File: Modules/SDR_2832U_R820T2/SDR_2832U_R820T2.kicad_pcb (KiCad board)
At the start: 2 copper layers, 140 parts, among them J1 2.54 Pins, J10 2.54 Pins, J2 2.54 Pins, J3 SMA, J4 SMA, J5 USB_C_Receptacle_USB2.0_16P, J6 SMA, J7 SMA, J8 SMA, J9 2.54 Sockets, Q1 GSFJ0300, T1 DXW21BN2511NL, U1 NCV68061, U2 NCV68061, U3 LM66200, U4 R820T2, U5 AP2127K-ADJ, U6 RTL2832U, U7 M24C02-WMN

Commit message: PCB progress
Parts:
- added C49: 100n, libraries:Worthington_C_Narrow_0201, F.Cu at (188.6, 72.3)
- added C50: 100n, libraries:Worthington_C_Narrow_0201, F.Cu at (192.6, 70.9)
- added C51: 100n, libraries:Worthington_C_Narrow_0201, F.Cu at (188.6, 74.6)
- added C52: 47u, libraries:Worthington_C_Narrow_0603, F.Cu at (199.4, 61.4)
- C10, C11, C12, C13, C14, C15, C17, C18, C19, C20, C22, C27, C28, C29, C3, C30, C31, C32, C33, C34, C35, C36, C37, C38, C39, C40, C41, C42, C43, C44, C45, C46, C47, C48, C6, C7, C8, C9: footprint libraries:Worthington_C_0201 -> libraries:Worthington_C_Narrow_0201
- C16, C21, C24, C25, C26, C4, C5: footprint libraries:Worthington_C_0402 -> libraries:Worthington_C_Narrow_0402
- C2: footprint libraries:Worthington_C_0402_0603 -> libraries:Worthington_C_Narrow_0402_0603
- J1, J2: moved to B.Cu
- J3, J6, J7: footprint Connector_Coaxial:SMA_Molex_73251-2200_Horizontal -> Connector_Coaxial:SMA_Amphenol_132289_EdgeMount
- J4: renamed from J8; footprint Connector_Coaxial:SMA_Molex_73251-2200_Horizontal -> Connector_Coaxial:SMA_Amphenol_132289_EdgeMount
- J5: footprint Connector_USB:USB_C_Receptacle_Amphenol_124019772112A -> Connector_USB:USB_C_Receptacle_GCT_USB4105-xx-A_16P_TopMnt_Horizontal
- J8: renamed from J4; footprint Connector_Coaxial:SMA_Molex_73251-2200_Horizontal -> Connector_Coaxial:SMA_Amphenol_132289_EdgeMount
- L1, L2, L3: footprint libraries:Worthington_L_0603_RF -> libraries:Worthington_L_Narrow_0603_RF
- R1, R10, R11, R12, R13, R14, R15, R16, R17, R18, R19, R2, R20, R21, R22, R23, R24, R25, R26, R27, R28, R29, R3, R4, R5, R6, R7, R8, R9: footprint libraries:Worthington_R_0201 -> libraries:Worthington_R_Narrow_0201
- moved J3 130.7 mm to (215.8, 86.9)
- moved C12 110.4 mm to (195.0, 79.3)
- moved C34 109.5 mm to (198.5, 62.2), turned to 90 degrees
- moved C15 109.4 mm to (195.0, 79.9)
- moved C19 108.7 mm to (195.0, 80.8)
- moved C35 108.6 mm to (197.6, 63.7)
- moved C9 108.6 mm to (192.4, 84.0), turned to -90 degrees
- moved C6 108.4 mm to (192.4, 76.2), turned to -90 degrees
- moved C36 108.1 mm to (197.1, 66.5)
- moved C28 107.5 mm to (194.1, 69.1), turned to -90 degrees
- moved C1 106.4 mm to (185.0, 51.2), turned to -90 degrees
- moved C11 106.3 mm to (190.8, 76.2), turned to 90 degrees
- moved C14 105.2 mm to (189.6, 76.2), turned to -90 degrees
- moved C46 104.6 mm to (195.2, 59.1), turned to 90 degrees
- moved C13 104.5 mm to (189.1, 76.2), turned to -90 degrees
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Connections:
- J4 pad 1: /RTL_CLK_IN -> /28.8MHz_CLK_IN
- J8 pad 1: /28.8MHz_CLK_IN -> /RTL_CLK_IN
- T1 pad 1: GND -> /RF_IN_LOW
- T1 pad 2: /RF_IN_LOW -> GND
- T1 pad 3: /IF_Q+ -> /IF_Q-
- T1 pad 4: /IF_Q- -> /IF_Q+
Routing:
- net GND: track 0.00 -> 38.1 mm, vias 0 -> 21
- net /RTL_1V2: track 0.00 -> 31.0 mm, vias 0 -> 9
- net +3V3: track 0.00 -> 27.4 mm, vias 0 -> 10
- net /IF_Q+: track 0.00 -> 20.7 mm
- net /RF_IN_HIGH: track 0.00 -> 20.3 mm
- net /IF_Q-: track 0.00 -> 19.9 mm
- net /RTL_1V2_OUT: track 0.00 -> 18.1 mm
- net /USB_SDR_D-: track 0.00 -> 17.3 mm, vias 0 -> 2
- net /USB_SDR_D+: track 0.00 -> 17.0 mm
- net /IF_I-: track 0.00 -> 5.55 mm
- net /IF_I+: track 0.00 -> 5.55 mm
- net /RF_IN_LOW: track 0.00 -> 5.33 mm
- net Net-(C31-Pad1): track 0.00 -> 5.09 mm, vias 0 -> 2
- net Net-(C30-Pad1): track 0.00 -> 5.09 mm, vias 0 -> 2
- net /GPIO1: track 0.00 -> 5.05 mm
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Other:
- board outline added: 53.1 x 46.1 mm
- copper layers 2 -> 4

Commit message: PCB progress
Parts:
- removed DN1: D3V3X8U9LP3810, Package_DFN_QFN:Diodes_UDFN3810-9_TYPE_B
- removed TP1, TP2, TP4, TP7, TP8, TP9: TestPoint, TestPoint:TestPoint_Keystone_5000-5004_Miniature
- added C53: 100n, libraries:Worthington_C_Narrow_0201, F.Cu at (207.5, 63.1)
- added D17: PUSB3FR4, Package_DFN_QFN:Diodes_UDFN-10_1x2.5mm_P0.5mm, F.Cu at (174.8, 82.5)
- added D18: PUSB3FR4, Package_DFN_QFN:Diodes_UDFN-10_1x2.5mm_P0.5mm, F.Cu at (174.8, 57.1)
- added J11: 2.54 Pins, Connector_PinHeader_2.54mm:PinHeader_1x04_P2.54mm_Vertical, F.Cu at (177.8, 53.3)
- D2, D5, D8, J4, J6, J8: moved to B.Cu
- D3: value SM05CN-SL -> DF3A6.8LFV,L3F; footprint Package_TO_SOT_SMD:SOT-23 -> Package_TO_SOT_SMD:SOT-723
- J10: footprint Connector_PinHeader_2.54mm:PinHeader_2x04_P2.54mm_Vertical -> Connector_PinHeader_2.54mm:PinHeader_1x04_P2.54mm_Vertical
- moved RN1 118.8 mm to (200.8, 52.5), turned to -90 degrees
- moved U1 118.1 mm to (203.8, 83.8)
- moved U2 117.1 mm to (207.3, 83.8), turned to 180 degrees
- moved R6 113.8 mm to (207.3, 77.1), turned to -90 degrees
- moved RN2 112.9 mm to (200.8, 57.8), turned to -90 degrees
- moved R12 111.9 mm to (205.4, 71.6), turned to 180 degrees
- moved R11 110.8 mm to (204.4, 71.6), turned to 180 degrees
- moved R29 106.6 mm to (204.3, 63.3), turned to 90 degrees
- moved R13 106.2 mm to (201.8, 73.5), turned to -90 degrees
- moved R27 105.7 mm to (203.8, 63.3), turned to 90 degrees
- moved U7 105.5 mm to (205.3, 59.1), turned to -90 degrees
- moved D12 103.7 mm to (180.7, 53.3), turned to 180 degrees
- moved D11 101.5 mm to (180.7, 55.9), turned to 180 degrees
- moved C23 100.9 mm to (201.4, 76.4), turned to -90 degrees
- moved Q1 100.6 mm to (205.5, 79.9)
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- renumbered TP14 to TP12, TP12 to TP14
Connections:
- D10 pad 2: /GPIO7 -> /GPIO6
- D11 pad 2: /GPIO7 -> /GPIO5
- D12 pad 2: /GPIO7 -> /GPIO4
- D13 pad 2: /GPIO7 -> /GPIO3
- D14 pad 2: /GPIO7 -> /GPIO2
- D15 pad 2: /GPIO7 -> /GPIO1
- D16 pad 2: /GPIO7 -> /GPIO0
- RN1 pad 5: unconnected-(RN1-Pad5) -> Net-(U7-E0)
- RN1 pad 6: Net-(U7-E2) -> Net-(U7-E1)
- RN1 pad 8: Net-(RN2A-4) -> unconnected-(RN1-Pad8)
- RN2 pad 1: Net-(RN2A-4) -> unconnected-(RN2A-4-Pad1)
- RN2 pad 3: Net-(U7-E2) -> Net-(U7-E1)
- RN2 pad 4: unconnected-(RN2-Pad4) -> Net-(U7-E0)
- RN3 pad 1: Net-(D9-K) -> Net-(D12-K)
- RN3 pad 2: Net-(D10-K) -> Net-(D11-K)
- RN3 pad 3: Net-(D11-K) -> Net-(D10-K)
- RN3 pad 4: Net-(D12-K) -> Net-(D9-K)
- RN4 pad 1: Net-(D13-K) -> Net-(D16-K)
- RN4 pad 2: Net-(D14-K) -> Net-(D15-K)
- RN4 pad 3: Net-(D15-K) -> Net-(D14-K)
- RN4 pad 4: Net-(D16-K) -> Net-(D13-K)
- TP12 pad 1: /EEPROM_SCL -> /EEPROM_SDA
- TP14 pad 1: /EEPROM_SDA -> /EEPROM_SCL
- U1 pad 1: VUSB -> GND
- U1 pad 2: Net-(Q1A-G) -> GND
- U1 pad 3: Net-(Q1A-D) -> VUSB
- U1 pad 4: VUSB -> Net-(Q1A-D)
- U1 pad 5: GND -> Net-(Q1A-G)
- U2 pad 1: Net-(J2-Pin_2) -> GND
- U2 pad 2: Net-(Q1B-G) -> GND
- U2 pad 3: Net-(Q1B-D) -> Net-(J2-Pin_2)
- U2 pad 4: Net-(J2-Pin_2) -> Net-(Q1B-D)
- U2 pad 5: GND -> Net-(Q1B-G)
- U7 pad 1: Net-(RN2A-4) -> Net-(U7-E0)
- U7 pad 2: Net-(RN1B-5) -> Net-(U7-E1)
- U7 pad 3: Net-(U7-E2) -> Net-(RN1B-5)
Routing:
- net /GPIO1: track 5.05 -> 91.3 mm, vias 0 -> 2
- net /GPIO2: track 4.73 -> 89.7 mm, vias 0 -> 1
- net GND: track 38.1 -> 100.1 mm, vias 21 -> 55
- net /GPIO3: track 1.25 -> 49.7 mm, vias 1 -> 2
- net /RTL_CLK_IN: track 0.00 -> 38.7 mm, vias 0 -> 1
- net /GPIO7: track 4.90 -> 36.5 mm, vias 0 -> 1
- net /GPIO0: track 1.42 -> 32.9 mm, vias 1 -> 2
- net /28.8MHz_CLK_OUT: track 0.00 -> 30.0 mm, vias 0 -> 1
- net /GPIO6: track 4.90 -> 34.1 mm, vias 0 -> 1
- net /28.8MHz_CLK_IN: track 0.00 -> 27.7 mm, vias 0 -> 1
- net /TUNER_SDA: track 2.86 -> 29.3 mm, vias 0 -> 1
- net /GPIO4: track 4.56 -> 30.8 mm, vias 0 -> 1
- net /IF_AGC_OUT: track 0.52 -> 25.7 mm, vias 0 -> 1
- net /GPIO5: track 3.95 -> 28.4 mm, vias 0 -> 1
- net +3V3: track 27.4 -> 51.8 mm, vias 10 -> 22
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- added copper zone on In2.Cu, net +3V3
- added copper zone on B.Cu, net /RTL_1V2
- added copper zone on B.Cu, net GND
- added copper zone on F.Cu, net GND
- added copper zone on In1.Cu, net GND
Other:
- board size 53.1 x 46.1 mm -> 53.1 x 46.4 mm

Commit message: PCB Layout Completed
Now I need to do the silkscreen stuffs...
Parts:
- added R30: 33?, libraries:Worthington_R_Narrow_0201, F.Cu at (186.5, 63.0)
- added R31: 33?, libraries:Worthington_R_Narrow_0201, F.Cu at (186.5, 63.6)
- moved D7 2.55 mm to (203.0, 72.2)
- moved C23 1.38 mm to (202.3, 75.4)
- moved C5 1.38 mm to (203.8, 76.2)
- moved D4 1.38 mm to (205.8, 74.7)
- moved Q1 1.38 mm to (206.5, 78.9)
- moved R6 1.38 mm to (208.3, 76.1)
- moved U2 1.38 mm to (208.3, 82.8)
- moved U3 1.38 mm to (206.5, 76.6)
- moved U5 1.38 mm to (205.8, 72.6)
- moved C16 1.38 mm to (208.4, 73.1)
- moved C4 1.38 mm to (208.8, 77.9)
- moved R11 1.38 mm to (205.3, 70.6)
- moved R12 1.38 mm to (206.3, 70.6)
- moved U1 1.38 mm to (204.7, 82.8)
- moved C34 0.71 mm to (199.2, 62.2)
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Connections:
- D7 pad 1: Net-(D7-K) -> GND
- D7 pad 2: +3V3 -> Net-(D7-A)
- R13 pad 1: Net-(D7-K) -> +3V3
- R13 pad 2: GND -> Net-(D7-A)
- U6 pad 40: /USB_SDR_D+ -> Net-(U6-USB_DP)
- U6 pad 41: /USB_SDR_D- -> Net-(U6-USB_DM)
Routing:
- net VUSB: track 18.3 -> 184.4 mm, vias 5 -> 11
- net /GPIO1: track 91.3 -> 69.3 mm
- net /GPIO2: track 89.7 -> 68.0 mm
- net Net-(J5-SHIELD): track 0.00 -> 21.1 mm
- net GND: track 100.1 -> 121.2 mm, vias 55 -> 207
- net /RTL_1V2: track 32.4 -> 49.5 mm, vias 9 -> 17
- net Net-(Q1B-D): track 20.7 -> 31.5 mm
- net +3V3: track 51.8 -> 60.8 mm, vias 22 -> 24
- net /EEPROM_SCL: track 17.5 -> 21.7 mm
- net Net-(U6-USB_DP): track 0.00 -> 3.82 mm
- net Net-(Q1A-D): track 22.1 -> 25.4 mm
- net /GPIO0: track 32.9 -> 36.1 mm
- net Net-(U6-USB_DM): track 0.00 -> 2.59 mm
- net Net-(J2-Pin_2): track 17.3 -> 19.8 mm
- net /RTL_1V2_OUT: track 18.1 -> 20.2 mm
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- added copper zone on In2.Cu, net Net-(J2-Pin_2)
- added copper zone on In2.Cu, net VUSB

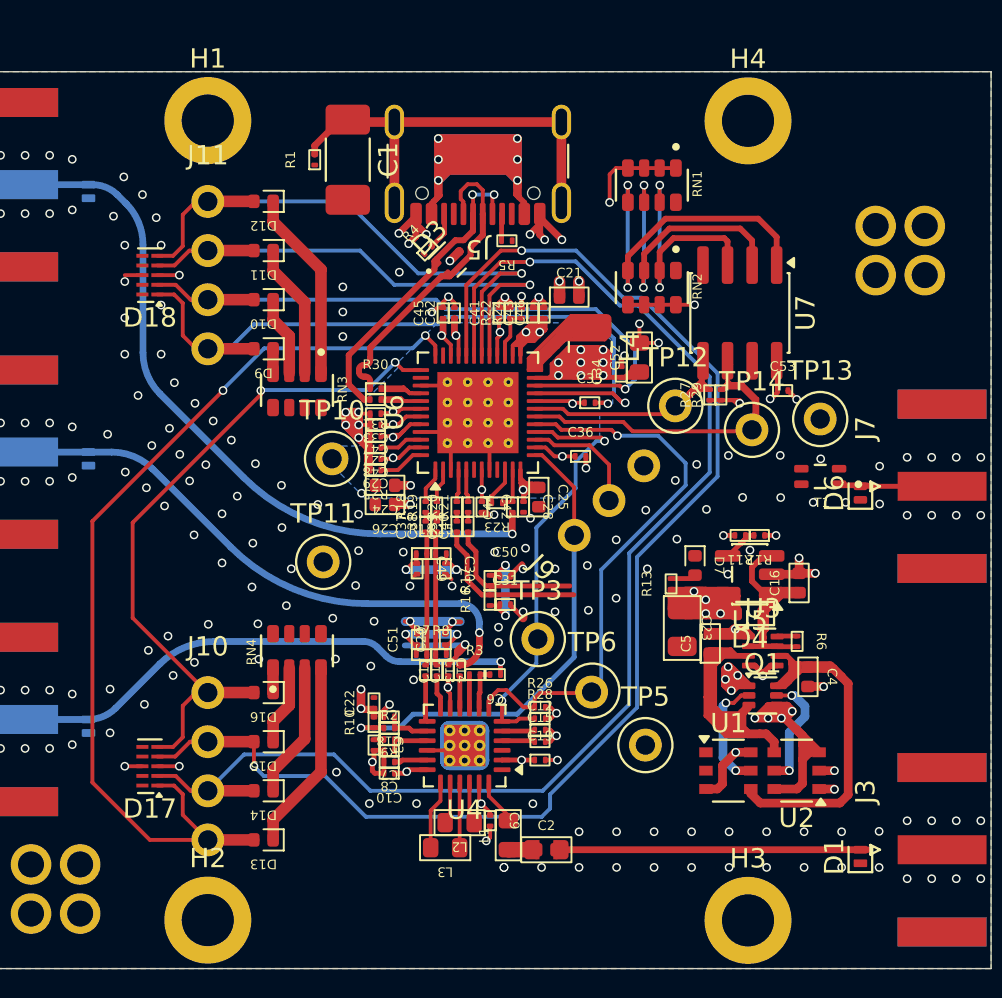
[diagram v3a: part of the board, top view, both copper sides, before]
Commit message: Silkscreen mostly done
Need to label the test points and connectors
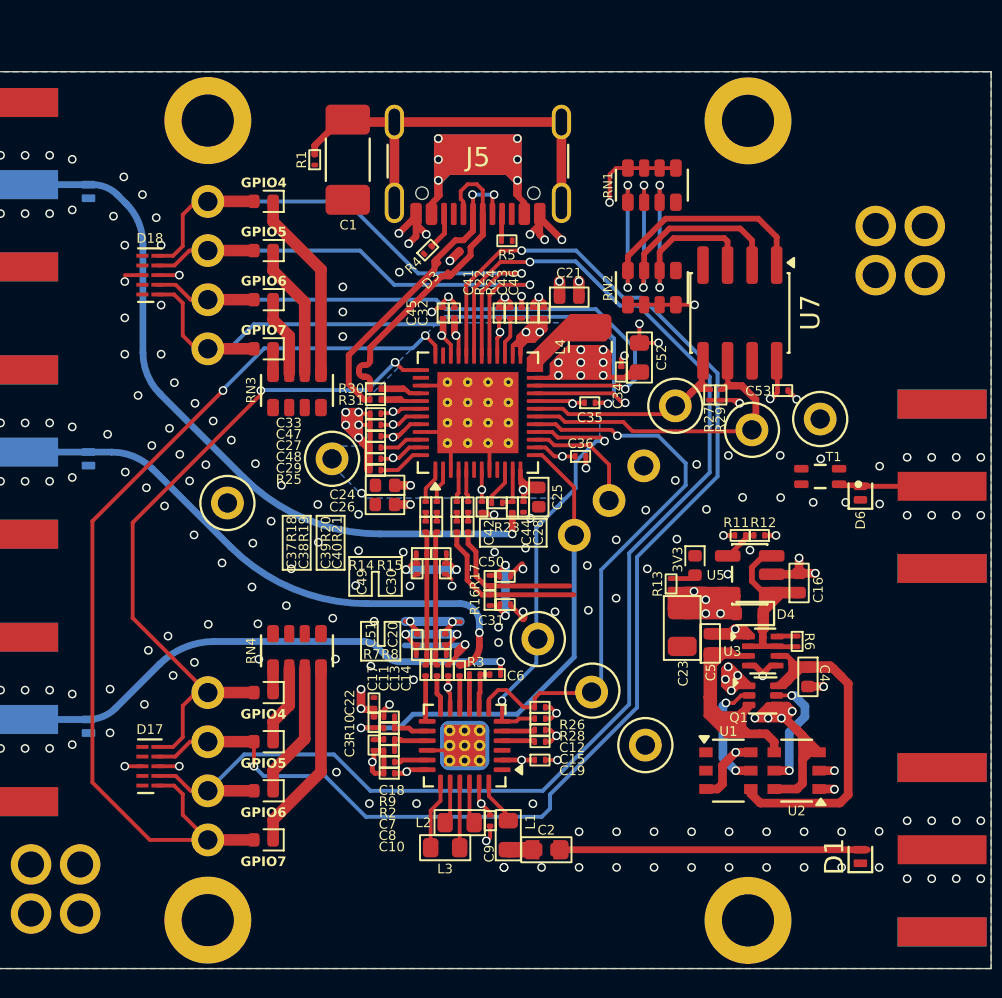
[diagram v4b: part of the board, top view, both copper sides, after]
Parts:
- added ?: , clipboard:0b796853-7cd1-42bf-9f29-726b268acd74, F.Cu at (205.2, 78.2)
- added ?: , clipboard:0b796853-7cd1-42bf-9f29-726b268acd74, F.Cu at (205.0, 75.8)
- moved TP11 5.82 mm to (178.8, 68.9)
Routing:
- net Net-(Q1B-D): track 31.5 -> 32.1 mm
- net GND: vias 207 -> 206
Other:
- board text added: "3V3"
- board text added: "GPIO4"
- board text added: "GPIO5"
- board text added: "GPIO6"
- board text added: "GPIO7"

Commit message: Added termination resistors to CLK lines
And did some silkscreen tweaks
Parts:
- added G***: LOGO, libraries:Logo_15mm_inv, B.Cu at (191.8, 64.4)
- added R32: 10k, libraries:Worthington_R_Narrow_0201, F.Cu at (194.1, 77.6)
- added R33: 10k, libraries:Worthington_R_Narrow_0201, F.Cu at (193.6, 77.6)
- added R34: 220, libraries:Worthington_R_Narrow_0201, F.Cu at (189.1, 77.6)
- added R35: 220, libraries:Worthington_R_Narrow_0201, F.Cu at (189.6, 77.6)
- added R36: 10k, libraries:Worthington_R_Narrow_0201, F.Cu at (193.0, 69.7)
- added R37: 10k, libraries:Worthington_R_Narrow_0201, F.Cu at (192.4, 69.7)
- added TP4: TestPoint, TestPoint:TestPoint_Keystone_5000-5004_Miniature, F.Cu at (213.5, 75.3)
- added TP7: TestPoint, TestPoint:TestPoint_Keystone_5000-5004_Miniature, F.Cu at (213.5, 79.6)
- moved C13 1.60 mm to (189.1, 76.0)
- moved C14 1.60 mm to (189.6, 76.0)
- moved TP3 1.37 mm to (196.2, 76.0)
- moved ? 0.88 mm to (206.0, 77.9), turned to -45 degrees
- moved TP6 0.72 mm to (198.4, 78.6)
- moved C6 0.36 mm to (192.4, 77.6), turned to -90 degrees
- moved TP12 0.23 mm to (201.8, 63.9)
- moved C42 0.15 mm to (191.8, 69.1)
- moved C20 0.13 mm to (190.2, 76.0)
- moved C51 0.13 mm to (188.5, 76.0)
- moved R23 0.08 mm to (192.7, 68.9)
- moved C9 0.05 mm to (192.4, 85.3)
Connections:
- C13 pad 2: Net-(U4-IF_P) -> Net-(C13-Pad2)
- C14 pad 2: Net-(U4-IF_N) -> Net-(C14-Pad2)
- R7 pad 2: /IF_I+ -> Net-(C13-Pad2)
- R8 pad 1: /IF_I- -> Net-(C14-Pad2)
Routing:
- net +5V_INT: track 14.7 -> 20.2 mm
- net GND: track 121.2 -> 124.7 mm, vias 206 -> 208
- net +3V3: track 60.8 -> 63.3 mm, vias 24 -> 26
- net /TUNER_SCL: track 22.5 -> 24.4 mm
- net Net-(U4-XIN/28.8MHz): track 2.27 -> 3.94 mm
- net /IF_AGC_OUT: track 25.4 -> 26.6 mm
- net /EEPROM_SDA: track 16.2 -> 17.4 mm
- net /RTL_CLK_IN: track 38.2 -> 39.4 mm
- net Net-(U6-XIN): track 2.22 -> 3.35 mm
- net Net-(C14-Pad2): track 0.00 -> 1.08 mm
- net Net-(C13-Pad2): track 0.00 -> 1.07 mm
- net Net-(C20-Pad1): track 5.26 -> 5.86 mm
- net /IF_I-: track 6.93 -> 6.37 mm
- net /IF_I+: track 6.93 -> 6.37 mm
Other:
- board text added: "+5V"
- board text added: "1V2"
- board text added: "2.0V_{pp}"
- board text added: "28.8 MHz"
- board text added: "3.3V_{pp}"
- board text added: "5V INT"
- board text added: "AGC"
- board text added: "CLK IN"
- board text added: "CLK OUT"
- board text added: "EEPROM"
- board text added: "GND"
- board text added: "GPIO0"
- board text added: "GPIO1"
- board text added: "GPIO2"
- board text added: "GPIO3"
- board text added: "I-CHANNEL"
- board text added: "IF"
- board text added: "MAX +10dBm"
- board text added: "Q-CHANNEL"
- board text added: "RF"
- board text added: "RF IN: DIRECT"
- board text added: "RF IN: TUNER"
- board text added: "RTL-SDR BREAKOUT"
- board text added: "RTL2832U"
- board text added: "RTL2832U & RT820T2"
- board text added: "SCL"
- board text added: "SDA"
- board text added: "TUNER"

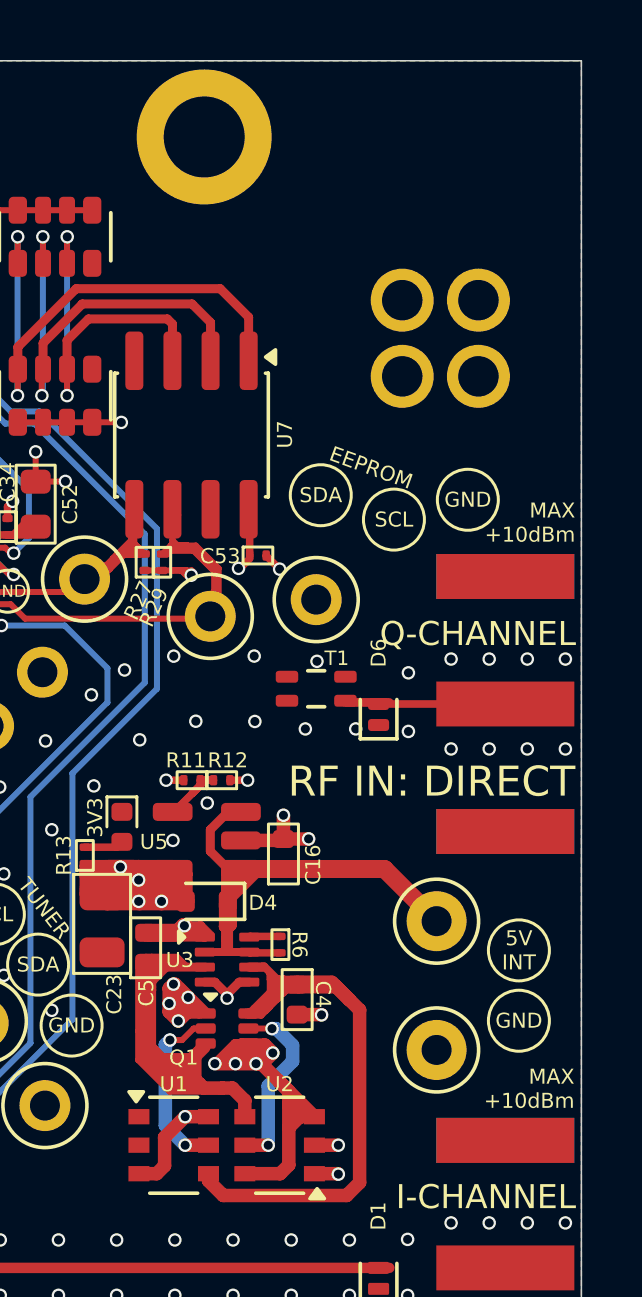
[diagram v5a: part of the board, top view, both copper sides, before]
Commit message: Added input power snubber
Just in case :P
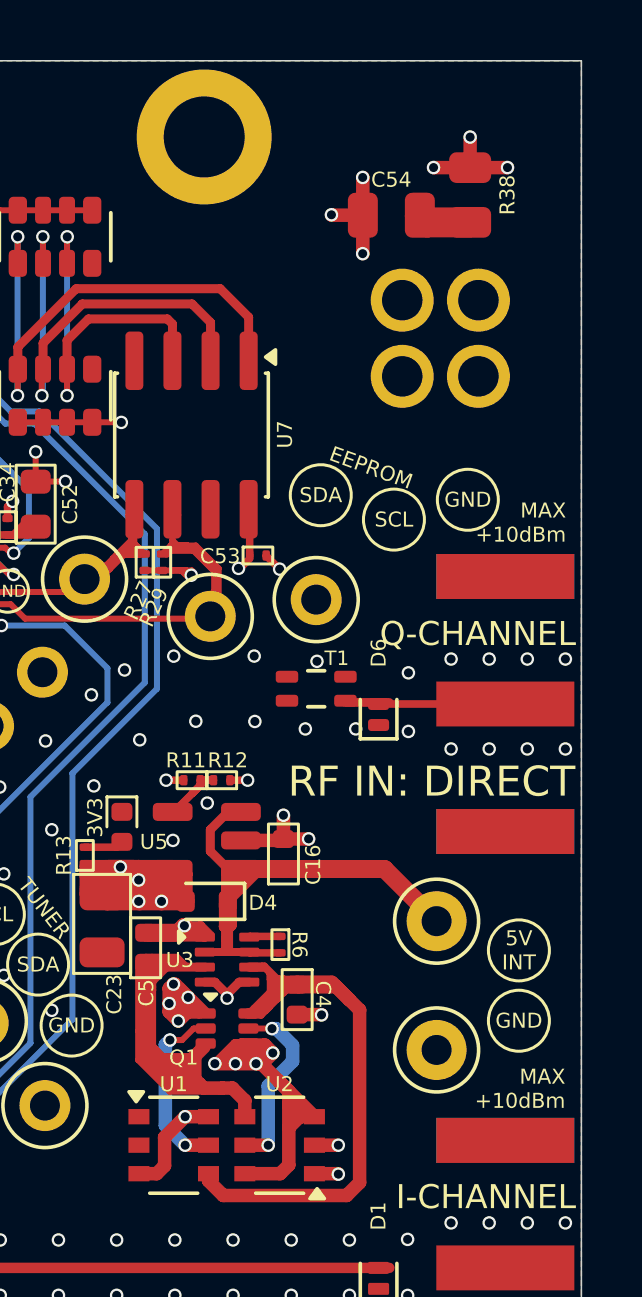
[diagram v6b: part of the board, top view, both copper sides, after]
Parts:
- added C54: 47u, libraries:Worthington_C_0805, F.Cu at (212.0, 51.8)
- added R38: 1R, Resistor_SMD:R_0805_2012Metric, F.Cu at (214.6, 51.1)
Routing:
- net VUSB: track 184.4 -> 188.0 mm, vias 11 -> 14
- net GND: track 124.7 -> 128.2 mm, vias 208 -> 211
- net Net-(C54-Pad2): track 0.00 -> 1.78 mm
